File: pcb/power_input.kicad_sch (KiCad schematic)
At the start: 9 parts

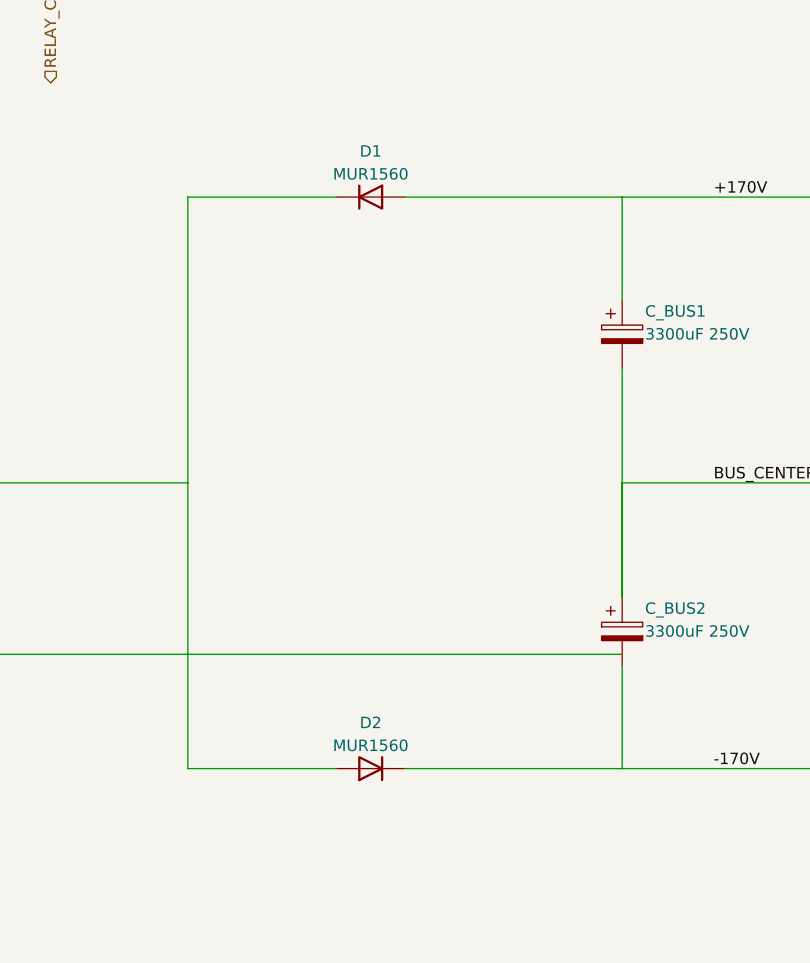
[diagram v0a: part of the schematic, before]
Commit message: fix: repair schematic wiring across all six PCB sheets
Systematic audit-and-verify pass over pcb/*.kicad_sch using a custom
union-find connectivity tracer, since KiCad's own ERC/netlist export only
confirm a file parses, not that intended nets are correct.

Found and fixed several serious latent bugs, none caught by prior tooling:
- mcu.kicad_sch: +3.3V shorted to two GPIOs; RTD_CS wired to the reset pin
  instead of a GPIO; all digital pins realigned to firmware/temper_pins.h
  after verifying firmware's pin choices against the real module symbol.
- half_bridge.kicad_sch: high-side IGBT wired backwards; bootstrap diode
  backwards; UCC21550 gate driver's entire control/supply side unwired.
- safety_interlock.kicad_sch: OCP comparator inputs swapped (inverted
  fault polarity); systematic wire-gap bug across comparators/logic gates;
  full NAND SR-latch rebuilt using real datasheet pin maps recovered from
  KiCad's own bundled multi-unit symbol libraries.
- power_management.kicad_sch: buck converter's SW pin was wired into the
  feedback divider instead of FB (coordinate typo); both ICs fully wired.
- power_input.kicad_sch: both mains rectifier diodes (D1, D2) in the
  voltage-doubler stage installed backwards, resolved via independent
  circuit-theory verification after design doc and atopile source
  disagreed with each other.
- sensing.kicad_sch: parse-blocking symbol bug; MAX31865 and ADUM1250
  fully wired (both were 100% unconnected).

user_interface.kicad_sch required no changes - confirmed already correct.

Documented the reusable techniques and root causes in docs/solutions/.

Co-Authored-By: Claude Sonnet 5 <noreply@anthropic.com>
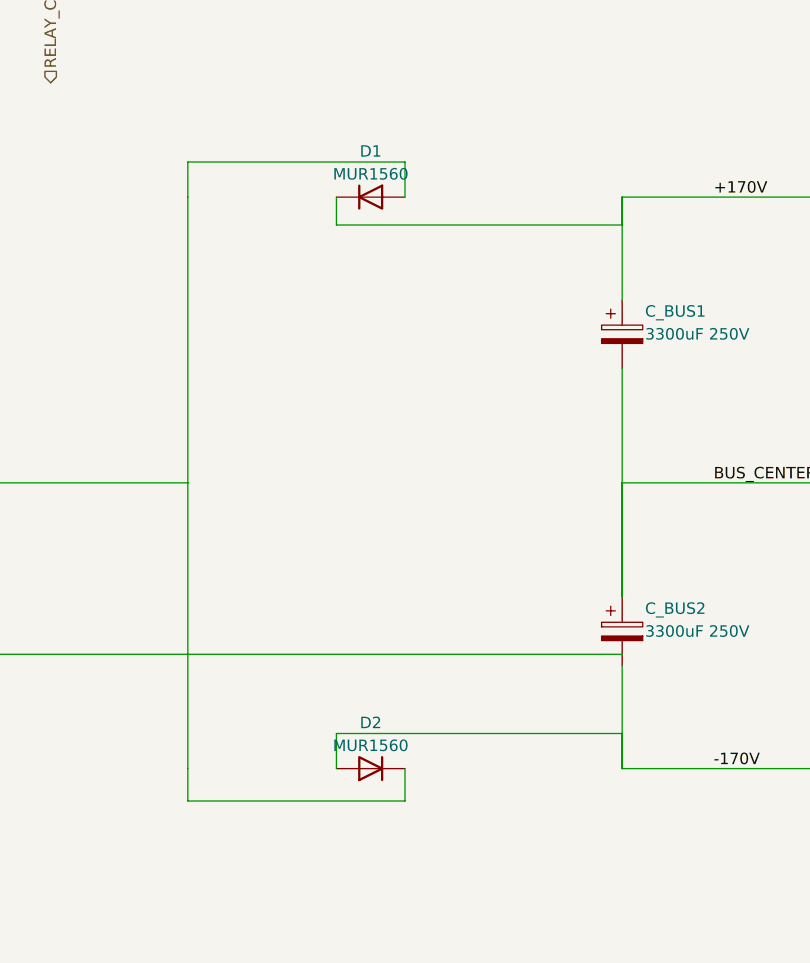
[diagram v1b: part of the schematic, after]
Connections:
- net DC_BUS+: now also D1.1 (K); no longer D1.2 (A)
- net DC_BUS-: now also D2.2 (A); no longer D2.1 (K)
- net at NTC_INRUSH.2, R_ZCD.1: now also D1.2 (A), D2.1 (K); no longer D1.1 (K), D2.2 (A)
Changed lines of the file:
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@@
   (wire (pts (xy 180.34 88.9) (xy 180.34 120.65)) (stroke (width 0) (type default)) (uuid "wire-junction-001"))
   (wire (pts (xy 180.34 120.65) (xy 180.34 152.4)) (stroke (width 0) (type default)) (uuid "wire-junction-002"))
-  (wire (pts (xy 180.34 88.9) (xy 196.85 88.9)) (stroke (width 0) (type default)) (uuid "wire-d1-001"))
-  (wire (pts (xy 204.47 88.9) (xy 228.6 88.9)) (stroke (width 0) (type default)) (uuid "wire-d1-002"))
+  (wire (pts (xy 180.34 88.9) (xy 180.34 85.0)) (stroke (width 0) (type default)) (uuid "wire-d1-001"))
+  (wire (pts (xy 180.34 85.0) (xy 204.47 85.0)) (stroke (width 0) (type default)) (uuid "wire-d1-001b"))
+  (wire (pts (xy 204.47 85.0) (xy 204.47 88.9)) (stroke (width 0) (type default)) (uuid "wire-d1-001c"))
+  (wire (pts (xy 196.85 88.9) (xy 196.85 92.0)) (stroke (width 0) (type default)) (uuid "wire-d1-002"))
+  (wire (pts (xy 196.85 92.0) (xy 228.6 92.0)) (stroke (width 0) (type default)) (uuid "wire-d1-002b"))
+  (wire (pts (xy 228.6 92.0) (xy 228.6 88.9)) (stroke (width 0) (type default)) (uuid "wire-d1-002c"))
   (wire (pts (xy 228.6 88.9) (xy 228.6 100.33)) (stroke (width 0) (type default)) (uuid "wire-d1-003"))
   (wire (pts (xy 228.6 88.9) (xy 251.46 88.9)) (stroke (width 0) (type default)) (uuid "wire-d1-004"))
   (wire (pts (xy 251.46 88.9) (xy 251.46 100.33)) (stroke (width 0) (type default)) (uuid "wire-d1-005"))
   (wire (pts (xy 251.46 88.9) (xy 279.4 88.9)) (stroke (width 0) (type default)) (uuid "wire-d1-006"))
-  (wire (pts (xy 180.34 152.4) (xy 196.85 152.4)) (stroke (width 0) (type default)) (uuid "wire-d2-001"))
-  (wire (pts (xy 204.47 152.4) (xy 228.6 152.4)) (stroke (width 0) (type default)) (uuid "wire-d2-002"))
+  (wire (pts (xy 180.34 152.4) (xy 180.34 156.0)) (stroke (width 0) (type default)) (uuid "wire-d2-001"))
+  (wire (pts (xy 180.34 156.0) (xy 204.47 156.0)) (stroke (width 0) (type default)) (uuid "wire-d2-001b"))
+  (wire (pts (xy 204.47 156.0) (xy 204.47 152.4)) (stroke (width 0) (type default)) (uuid "wire-d2-001c"))
+  (wire (pts (xy 196.85 152.4) (xy 196.85 148.5)) (stroke (width 0) (type default)) (uuid "wire-d2-002"))
+  (wire (pts (xy 196.85 148.5) (xy 228.6 148.5)) (stroke (width 0) (type default)) (uuid "wire-d2-002b"))
+  (wire (pts (xy 228.6 148.5) (xy 228.6 152.4)) (stroke (width 0) (type default)) (uuid "wire-d2-002c"))
   (wire (pts (xy 228.6 140.97) (xy 228.6 152.4)) (stroke (width 0) (type default)) (uuid "wire-d2-003"))
   (wire (pts (xy 228.6 152.4) (xy 251.46 152.4)) (stroke (width 0) (type default)) (uuid "wire-d2-004"))

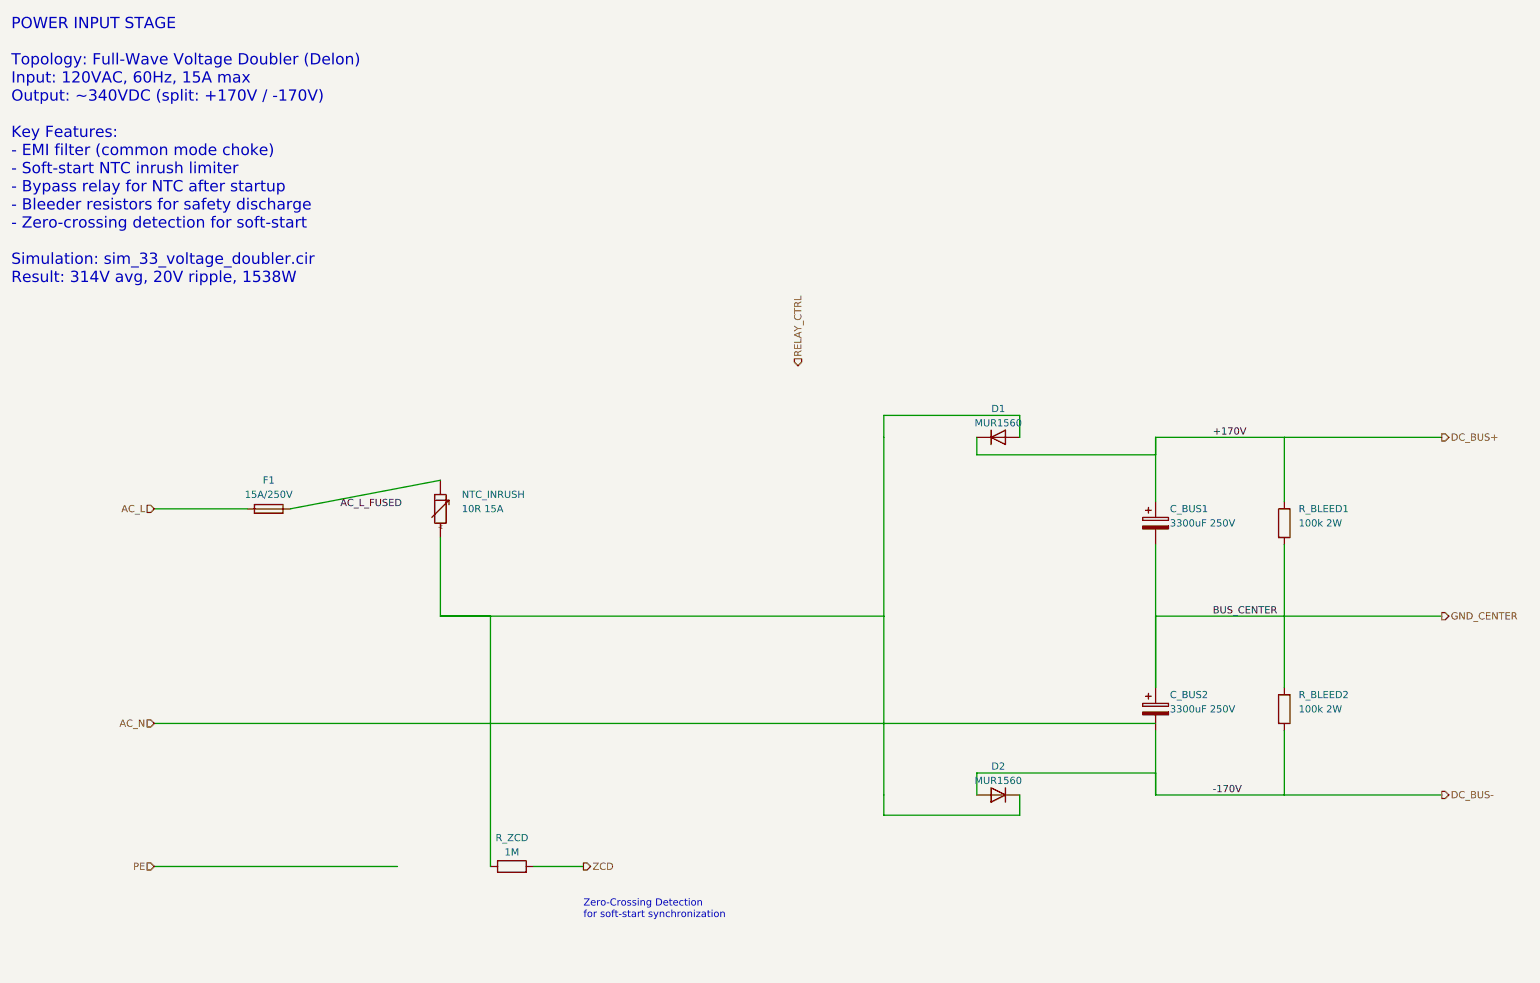
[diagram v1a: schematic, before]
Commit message: fix: remediate 8 remaining open schematic items (relay driver, R_BURDEN dedup, MAX31865 footprint, isolated 5V, RUNAWAY_CUT/RESET_N, fault-LED taps)
Closes out the open-questions list from the prior schematic repair session
(docs/plans/2026-07-14-001-fix-schematic-open-items-remediation-plan.md):

- Fix AC_N routing to the doubler's center tap (independently re-derived via
  KCL before editing mains wiring), in both the schematic and elec/src
- Give GND_CENTER a real ground connection and a Y2-capacitor PE bond;
  resolved a real conflict between two hardware docs on where system
  ground lives, using the generative .ato source as an independent tiebreaker
- Add the NTC bypass relay + low-side MOSFET driver circuit for RELAY_CTRL
- Consolidate duplicate R_BURDEN into Half_Bridge; found the surviving
  copy's signal/reference pins were swapped
- Fix the MAX31865 footprint (wrong package entirely) and add the missing
  pcb/fp-lib-table
- Add the isolated +5V_ISO DC-DC supply for the I2C isolator's far side
- Remove vestigial MCU_ENABLE; wire the real RUNAWAY_CUT net using the
  74HC4075's actual datasheet-sourced gate mapping, not pin-adjacency guesses
- Fix User_Interface's stale root pins and hierarchize the four fault-LED
  taps in Safety_Interlock (all four were floating, not just WDT_FAULT)

Every unit verified via union-find connectivity trace before and after
writing, plus a full-project kicad-cli parse/ERC pass. Three bugs were
self-caught by that discipline before landing: a lib_symbols block placed
outside its container (broke the parser outright), a RESET_N direction
mismatch, and a shared-sheet-edge routing overlap -- the latter two folded
into docs/solutions/tooling-decisions/kicad-schematic-connectivity-tracer.

Co-Authored-By: Claude Sonnet 5 <noreply@anthropic.com>
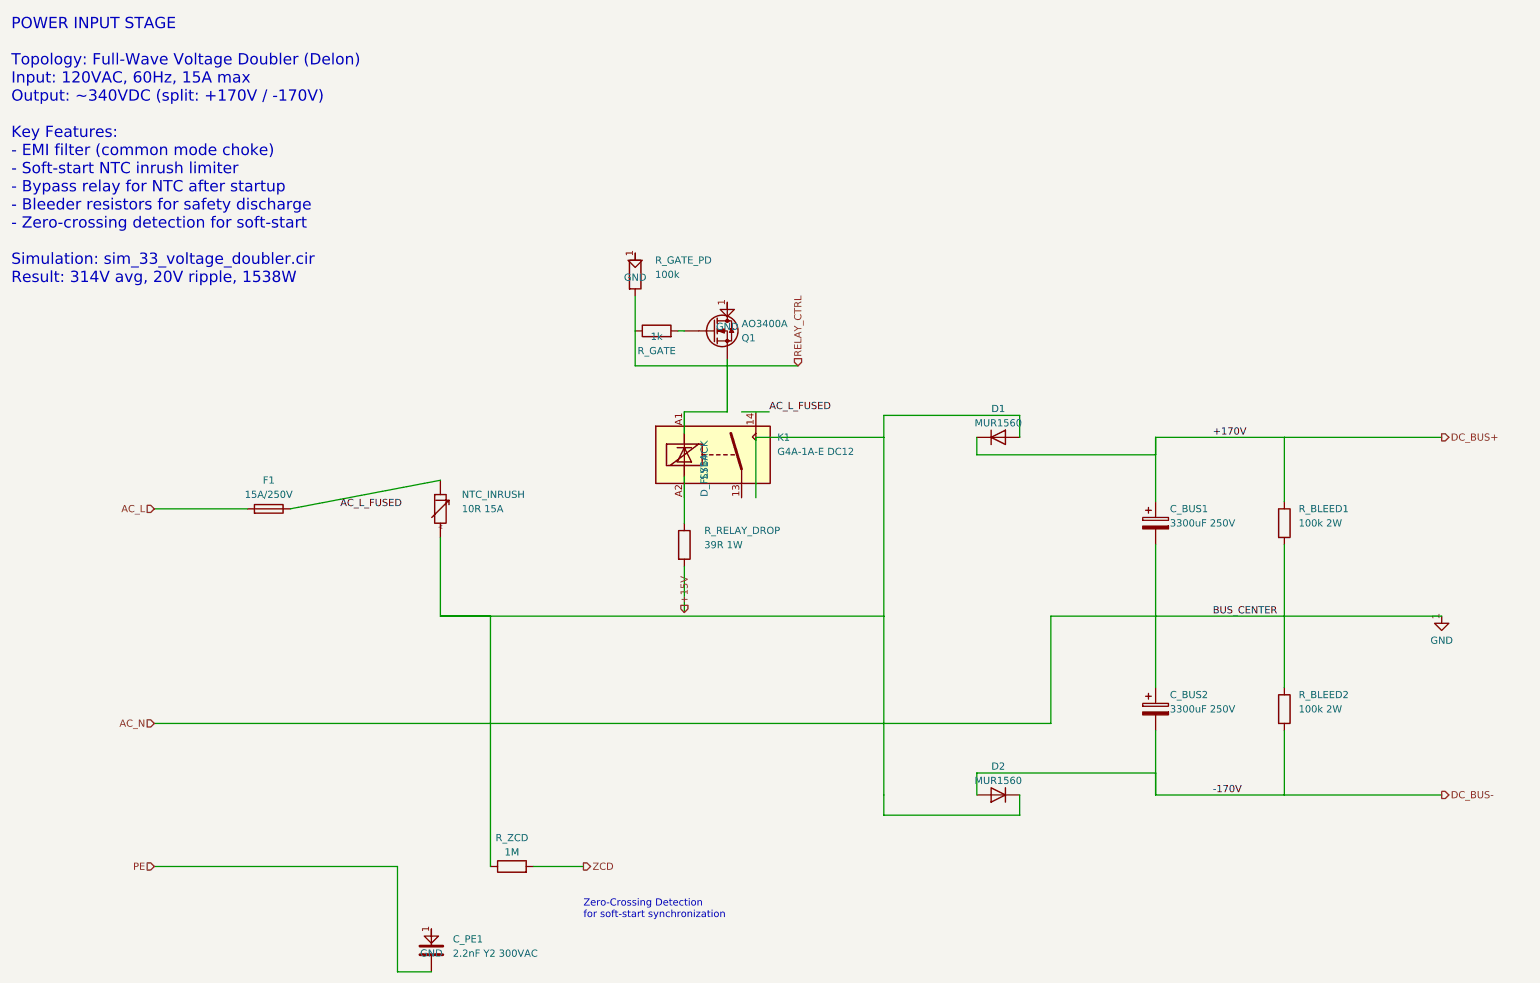
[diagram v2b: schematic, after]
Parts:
- added C_PE1: 2.2nF Y2 300VAC, Capacitor_THT:C_Disc_D10.5mm_W5.0mm_P7.50mm, symbol Device:C
- added D_FLYBACK: SS14, Diode_SMD:D_SMA, symbol Device:D
- added K1: G4A-1A-E DC12, Relay_THT:Relay_SPST_Omron-G4A-E, symbol Relay:Relay_SPST-NO
- added Q1: AO3400A, Package_TO_SOT_SMD:SOT-23, symbol Device:Q_NMOS
- added R_GATE: 1k, Resistor_SMD:R_0805_2012Metric, symbol Device:R
- added R_GATE_PD: 100k, Resistor_SMD:R_0805_2012Metric, symbol Device:R
- added R_RELAY_DROP: 39R 1W, Resistor_THT:R_Axial_DIN0207_L6.3mm_D2.5mm_P10.16mm_Horizontal, symbol Device:R
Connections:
- net PE: now also C_PE1.2
- net RELAY_CTRL: now also R_GATE.1, R_GATE_PD.2
- net GND_CENTER renamed GND
- net GND: now also C_PE1.1, Q1.D, R_GATE_PD.1
- new net: D_FLYBACK.1 (K), K1.A1, Q1.S
- new net: D_FLYBACK.2 (A), K1.A2, R_RELAY_DROP.1
- new net: Q1.G, R_GATE.2
- new net +15V: R_RELAY_DROP.2

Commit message: feat: hand-build custom footprints from real datasheets (relay, CT, DC-DC), fix stale footprint references
Draws the three custom footprints that were previously deferred as
"mechanical CAD work" -- .kicad_mod is the same S-expression text format
as .kicad_sch, and all three parts have public datasheets with real
mechanical dimensions:

- pcb/libs/temper.pretty/Relay_SPST_Omron-G4A-E.kicad_mod: Omron G4A-1A-E
  relay. Coil pins (6.35mm pitch) and #250 Faston contact terminals sourced
  from the official Omron datasheet. Confirmed via the datasheet's own
  Model Number Legend text (not an inferred drawing detail) that the
  contacts have zero PCB copper connection on this variant -- modeled as
  placeholder SMD pads for symbol/footprint pin-count parity only.
  Mounting-hole positions are flagged for a human visual cross-check
  against the datasheet before fabrication.
- pcb/libs/temper.pretty/CST-1005.kicad_mod: Triad Magnetics CST-1005
  current sense transformer. Secondary pin pitch, primary window diameter,
  and pin diameter are all high-confidence, unambiguous datasheet table
  values.
- pcb/libs/temper.pretty/Converter_DCDC_RECOM_RP-S.kicad_mod: RECOM RP-1505S
  isolated DC-DC. Best-sourced of the three -- clean table data including
  the real SIP7 populated-pin pattern (2 of 7 positions genuinely absent on
  the single-output variant), cross-checked via two independently-labeled
  span dimensions in the datasheet. Replaces a Footprint reference that
  pointed at a library entry that didn't exist in any installed KiCad
  library.

All three footprints' pad numbers were remapped to match the already-placed
KiCad symbols' generic pin numbering (not the datasheets' own silkscreen
pin numbers), with the real-part mapping documented in each file's descr
field, after catching that a naive 1:1 pad-number assumption would have
mismatched the symbols.

Also: elec/src/footprints.ato's separate (not yet build-wired) generative
CST1005_Footprint module had an unsourced p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
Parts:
- K1: footprint Relay_THT:Relay_SPST_Omron-G4A-E -> temper:Relay_SPST_Omron-G4A-E
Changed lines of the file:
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@@
     (property "Reference" "K1" (at 161.43 88.9 0) (effects (font (size 1.27 1.27)) (justify left)))
     (property "Value" "G4A-1A-E DC12" (at 161.43 91.44 0) (effects (font (size 1.27 1.27)) (justify left)))
-    (property "Footprint" "Relay_THT:Relay_SPST_Omron-G4A-E" (at 150.0 92.0 0) (effects (font (size 1.27 1.27)) hide))
+    (property "Footprint" "temper:Relay_SPST_Omron-G4A-E" (at 150.0 92.0 0) (effects (font (size 1.27 1.27)) hide))
     (property "MPN" "G4A-1A-E DC12" (at 150.0 92.0 0) (effects (font (size 1.27 1.27)) hide))
     (property "Manufacturer" "Omron" (at 150.0 92.0 0) (effects (font (size 1.27 1.27)) hide))
-    (property "Description" "NTC bypass relay, 20A/250VAC contacts, 12V/75mA coil. Footprint is a placeholder -- no G4A-1A-E footprint exists in any KiCad library; a custom footprint must be drawn (see plan U3 follow-up)." (at 150.0 92.0 0) (effects (font (size 1.27 1.27)) hide))
+    (property "Description" "NTC bypass relay, 20A/250VAC contacts, 12V/75mA coil. Custom footprint drawn from the real Omron datasheet at pcb/libs/temper.pretty/Relay_SPST_Omron-G4A-E.kicad_mod -- see that file's descr field for dimension sourcing and residual confidence notes (mounting-hole and tab-pad positions should be visually cross-checked against the datasheet before fabrication)." (at 150.0 92.0 0) (effects (font (size 1.27 1.27)) hide))
     (pin "13" (uuid "k1-pin13-uuid"))
     (pin "14" (uuid "k1-pin14-uuid"))
